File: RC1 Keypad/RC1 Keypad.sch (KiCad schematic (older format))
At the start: 24 parts

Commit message: Added RS/ST/SST to schematic
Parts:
- removed J?: KB, symbol Conn_02x05_Counter_Clockwise
- added D1: PWR, symbol LED_Small
- added J1: KB, symbol Conn_02x08_Counter_Clockwise
- added SW22: SST, symbol SW_SPST
- added SW23: RS, Button_Switch_Keyboard:SW_Cherry_MX_1.00u_PCB, symbol SW_Keyboard
- added SW24: ST, Button_Switch_Keyboard:SW_Cherry_MX_1.00u_PCB, symbol SW_Keyboard
- gave numbers to parts that had none: 23
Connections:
- net labels added: LED, RS, SST_IN, SST_OUT, ST, VCC
- wire segments 69 -> 85
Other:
- moved on the sheet: SW1, SW10, SW11, SW12, SW13, SW14, SW15, SW16, SW17, SW18, SW19, SW2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

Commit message: Keypad layout done
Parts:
- removed M1, M2: Mounting, Mounting:1pin, symbol Mounting
- D1: footprint (none) -> LEDs:LED_D5.0mm
- J1: footprint (none) -> Pin_Headers:Pin_Header_Straight_2x08_Pitch2.54mm
- SW22: footprint (none) -> Buttons_Switches_THT:SW_DIP_x1_W7.62mm_Slide
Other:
- note added: "RC-1 Hex keypad"
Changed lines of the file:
@@
 LIBS:valves
 LIBS:sw_keyboard
-LIBS:ZX Keyboard-cache
+LIBS:RC1 Keypad-cache
 EELAYER 25 0
 EELAYER END
@@
 Connection ~ 5225 4350
 $Comp
-L Mounting M2
-U 1 1 5D61DCEC
-P 11150 550
-F 0 "M2" H 11150 650 50  0001 C CNN
-F 1 "Mounting" H 11150 475 50  0001 C CNN
-F 2 "Mounting:1pin" H 11150 550 50  0001 C CNN
-F 3 "" H 11150 550 50  0001 C CNN
-	1    11150 550
-	1    0    0    -1
-$EndComp
-$Comp
-L Mounting M1
-U 1 1 5D61DCED
-P 11025 550
-F 0 "M1" H 11025 650 50  0001 C CNN
-F 1 "Mounting" H 11025 475 50  0001 C CNN
-F 2 "Mounting:1pin" H 11025 550 50  0001 C CNN
-F 3 "" H 11025 550 50  0001 C CNN
-	1    11025 550
-	1    0    0    -1
-$EndComp
-$Comp
 L SW_Keyboard SW13
 U 1 1 5D61DCC3
@@
 F 0 "SW22" H 6375 2350 50  0000 C CNN
 F 1 "SST" H 6375 2175 50  0000 C CNN
-F 2 "" H 6375 2225 50  0001 C CNN
+F 2 "Buttons_Switches_THT:SW_DIP_x1_W7.62mm_Slide" H 6375 2225 50  0001 C CNN
 F 3 "" H 6375 2225 50  0001 C CNN
 	1    6375 2225
@@
 F 0 "J1" H 5500 2775 50  0000 C CNN
 F 1 "KB" H 5500 2175 50  0000 C CNN
-F 2 "" H 5450 2525 50  0001 C CNN
+F 2 "Pin_Headers:Pin_Header_Straight_2x08_Pitch2.54mm" H 5450 2525 50  0001 C CNN
 F 3 "" H 5450 2525 50  0001 C CNN
 	1    5450 2525
@@
 F 0 "D1" H 6125 2475 50  0000 L CNN
 F 1 "PWR" H 6350 2475 50  0000 L CNN
-F 2 "" V 6275 2425 50  0001 C CNN
+F 2 "LEDs:LED_D5.0mm" V 6275 2425 50  0001 C CNN
 F 3 "" V 6275 2425 50  0001 C CNN
 	1    6275 2425
@@
 Wire Wire Line
 	6650 2225 6650 2325
+Text Notes 7350 7500 0    60   ~ 0
+RC-1 Hex keypad
 $EndSCHEMATC

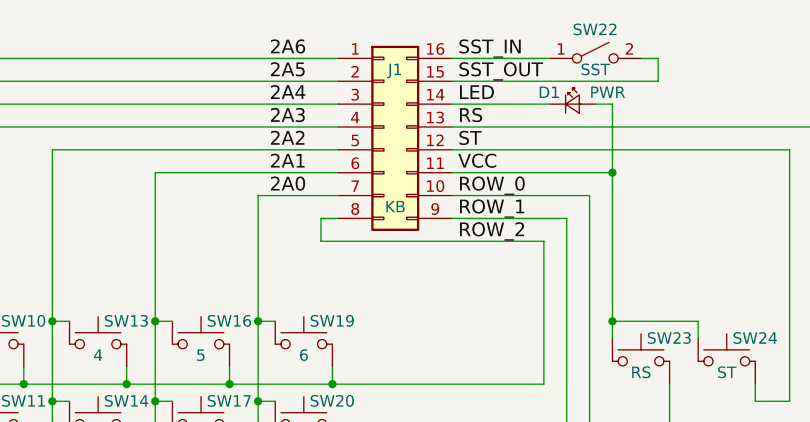
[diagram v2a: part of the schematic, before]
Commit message: Added UI signals to CPU board
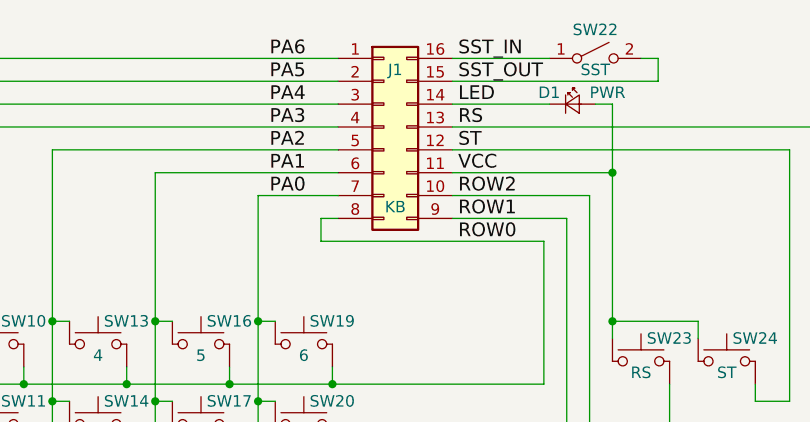
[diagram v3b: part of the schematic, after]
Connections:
- net 2A0 renamed PA0
- net 2A1 renamed PA1
- net 2A2 renamed PA2
- net 2A3 renamed PA3
- net 2A4 renamed PA4
- net 2A5 renamed PA5
- net 2A6 renamed PA6
- net ROW_0 renamed ROW2
- net ROW_1 renamed ROW1
- net ROW_2 renamed ROW0
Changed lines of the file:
@@
 	1    0    0    -1
 $EndComp
+Text Label 5775 3025 0    60   ~ 0
+ROW0
+Text Label 5775 2925 0    60   ~ 0
+ROW1
 Text Label 5775 2825 0    60   ~ 0
-ROW_0
-Text Label 5775 2925 0    60   ~ 0
-ROW_1
-Text Label 5775 3025 0    60   ~ 0
-ROW_2
+ROW2
 Wire Wire Line
 	2200 2225 5250 2225
@@
 	3550 2525 5250 2525
 Text Label 4950 2825 0    60   ~ 0
-2A0
+PA0
 Text Label 4950 2725 0    60   ~ 0
-2A1
+PA1
 Text Label 4950 2625 0    60   ~ 0
-2A2
+PA2
 Text Label 4950 2525 0    60   ~ 0
-2A3
+PA3
 Text Label 4950 2425 0    60   ~ 0
-2A4
+PA4
 Text Label 4950 2325 0    60   ~ 0
-2A5
+PA5
 Wire Wire Line
 	4000 2625 5250 2625
 Text Label 4950 2225 0    60   ~ 0
-2A6
+PA6
 $Comp
 L SW_Keyboard SW23

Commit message: Keypad SX layout done
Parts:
- removed SW22: SST, Buttons_Switches_THT:SW_DIP_x1_W7.62mm_Slide, symbol SW_SPST
- added M1, M2, M3, M4: Mounting, Mounting:1pin, symbol Mounting
- added SW22: SST, Pin_Headers:Pin_Header_Straight_1x03_Pitch2.54mm, symbol SW_SPDT
- SW1, SW10, SW11, SW12, SW13, SW14, SW15, SW16, SW17, SW18, SW19, SW2, SW20, SW21, SW23, SW24, SW3, SW4, SW5, SW6, SW7, SW8, SW9: footprint Button_Switch_Keyboard:SW_Cherry_MX_1.00u_PCB -> Buttons_Switches_THT:SW_PUSH_6mm
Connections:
- net SST_IN: now also SW22.2 (B)
- net SST_OUT: now also SW22.3 (C)
- no-connect marks 0 -> 1
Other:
- note added: "The keypad module for the RC One computer, has the classic KIM-1 layout with a\ncustom connector. This is the standard version using cheap tactile momentary buttons\nand is smaller [and cheaper to make] compared to the MX version."
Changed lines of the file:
@@
 LIBS:valves
 LIBS:sw_keyboard
+LIBS:mounting
 LIBS:RC1 Keypad-cache
 EELAYER 25 0
@@
 F 0 "SW16" H 4675 3575 50  0000 L CNN
 F 1 "5" H 4650 3425 50  0000 C CNN
-F 2 "Button_Switch_Keyboard:SW_Cherry_MX_1.00u_PCB" H 4650 3675 50  0001 C CNN
+F 2 "Buttons_Switches_THT:SW_PUSH_6mm" H 4650 3675 50  0001 C CNN
 F 3 "" H 4650 3675 50  0001 C CNN
 	1    4650 3475
@@
 F 0 "SW10" H 3775 3575 50  0000 L CNN
 F 1 "3" H 3750 3425 50  0000 C CNN
-F 2 "Button_Switch_Keyboard:SW_Cherry_MX_1.00u_PCB" H 3750 3675 50  0001 C CNN
+F 2 "Buttons_Switches_THT:SW_PUSH_6mm" H 3750 3675 50  0001 C CNN
 F 3 "" H 3750 3675 50  0001 C CNN
 	1    3750 3475
@@
 F 0 "SW7" H 3325 3575 50  0000 L CNN
 F 1 "2" H 3300 3425 50  0000 C CNN
-F 2 "Button_Switch_Keyboard:SW_Cherry_MX_1.00u_PCB" H 3300 3675 50  0001 C CNN
+F 2 "Buttons_Switches_THT:SW_PUSH_6mm" H 3300 3675 50  0001 C CNN
 F 3 "" H 3300 3675 50  0001 C CNN
 	1    3300 3475
@@
 F 0 "SW4" H 2875 3575 50  0000 L CNN
 F 1 "1" H 2850 3425 50  0000 C CNN
-F 2 "Button_Switch_Keyboard:SW_Cherry_MX_1.00u_PCB" H 2850 3675 50  0001 C CNN
+F 2 "Buttons_Switches_THT:SW_PUSH_6mm" H 2850 3675 50  0001 C CNN
 F 3 "" H 2850 3675 50  0001 C CNN
 	1    2850 3475
@@
 F 0 "SW12" H 3775 4275 50  0000 L CNN
 F 1 "DA" H 3750 4125 50  0000 C CNN
-F 2 "Button_Switch_Keyboard:SW_Cherry_MX_1.00u_PCB" H 3750 4375 50  0001 C CNN
+F 2 "Buttons_Switches_THT:SW_PUSH_6mm" H 3750 4375 50  0001 C CNN
 F 3 "" H 3750 4375 50  0001 C CNN
 	1    3750 4175
@@
 F 0 "SW3" H 2425 4275 50  0000 L CNN
 F 1 "E" H 2400 4125 50  0000 C CNN
-F 2 "Button_Switch_Keyboard:SW_Cherry_MX_1.00u_PCB" H 2400 4375 50  0001 C CNN
+F 2 "Buttons_Switches_THT:SW_PUSH_6mm" H 2400 4375 50  0001 C CNN
 F 3 "" H 2400 4375 50  0001 C CNN
 	1    2400 4175
@@
 F 0 "SW6" H 2875 4275 50  0000 L CNN
 F 1 "F" H 2850 4125 50  0000 C CNN
-F 2 "Button_Switch_Keyboard:SW_Cherry_MX_1.00u_PCB" H 2850 4375 50  0001 C CNN
+F 2 "Buttons_Switches_THT:SW_PUSH_6mm" H 2850 4375 50  0001 C CNN
 F 3 "" H 2850 4375 50  0001 C CNN
 	1    2850 4175
@@
 F 0 "SW20" H 5125 3925 50  0000 L CNN
 F 1 "D" H 5100 3775 50  0000 C CNN
-F 2 "Button_Switch_Keyboard:SW_Cherry_MX_1.00u_PCB" H 5100 4025 50  0001 C CNN
+F 2 "Buttons_Switches_THT:SW_PUSH_6mm" H 5100 4025 50  0001 C CNN
 F 3 "" H 5100 4025 50  0001 C CNN
 	1    5100 3825
@@
 F 0 "SW11" H 3775 3925 50  0000 L CNN
 F 1 "A" H 3750 3775 50  0000 C CNN
-F 2 "Button_Switch_Keyboard:SW_Cherry_MX_1.00u_PCB" H 3750 4025 50  0001 C CNN
+F 2 "Buttons_Switches_THT:SW_PUSH_6mm" H 3750 4025 50  0001 C CNN
 F 3 "" H 3750 4025 50  0001 C CNN
 	1    3750 3825
@@
 F 0 "SW19" H 5125 3575 50  0000 L CNN
 F 1 "6" H 5100 3425 50  0000 C CNN
-F 2 "Button_Switch_Keyboard:SW_Cherry_MX_1.00u_PCB" H 5100 3675 50  0001 C CNN
+F 2 "Buttons_Switches_THT:SW_PUSH_6mm" H 5100 3675 50  0001 C CNN
 F 3 "" H 5100 3675 50  0001 C CNN
 	1    5100 3475
@@
 F 0 "SW2" H 2425 3925 50  0000 L CNN
 F 1 "7" H 2400 3775 50  0000 C CNN
-F 2 "Button_Switch_Keyboard:SW_Cherry_MX_1.00u_PCB" H 2400 4025 50  0001 C CNN
+F 2 "Buttons_Switches_THT:SW_PUSH_6mm" H 2400 4025 50  0001 C CNN
 F 3 "" H 2400 4025 50  0001 C CNN
 	1    2400 3825
@@
 F 0 "SW5" H 2875 3925 50  0000 L CNN
 F 1 "8" H 2850 3775 50  0000 C CNN
-F 2 "Button_Switch_Keyboard:SW_Cherry_MX_1.00u_PCB" H 2850 4025 50  0001 C CNN
+F 2 "Buttons_Switches_THT:SW_PUSH_6mm" H 2850 4025 50  0001 C CNN
 F 3 "" H 2850 4025 50  0001 C CNN
 	1    2850 3825
@@
 F 0 "SW8" H 3325 3925 50  0000 L CNN
 F 1 "9" H 3300 3775 50  0000 C CNN
-F 2 "Button_Switch_Keyboard:SW_Cherry_MX_1.00u_PCB" H 3300 4025 50  0001 C CNN
+F 2 "Buttons_Switches_THT:SW_PUSH_6mm" H 3300 4025 50  0001 C CNN
 F 3 "" H 3300 4025 50  0001 C CNN
 	1    3300 3825
@@
 F 0 "SW1" H 2425 3575 50  0000 L CNN
 F 1 "Ø" H 2400 3425 50  0000 C CNN
-F 2 "Button_Switch_Keyboard:SW_Cherry_MX_1.00u_PCB" H 2400 3675 50  0001 C CNN
+F 2 "Buttons_Switches_THT:SW_PUSH_6mm" H 2400 3675 50  0001 C CNN
 F 3 "" H 2400 3675 50  0001 C CNN
 	1    2400 3475
@@
 F 0 "SW9" H 3325 4275 50  0000 L CNN
 F 1 "AD" H 3300 4125 50  0000 C CNN
-F 2 "Button_Switch_Keyboard:SW_Cherry_MX_1.00u_PCB" H 3300 4375 50  0001 C CNN
+F 2 "Buttons_Switches_THT:SW_PUSH_6mm" H 3300 4375 50  0001 C CNN
 F 3 "" H 3300 4375 50  0001 C CNN
 	1    3300 4175
@@
 F 0 "SW14" H 4225 3925 50  0000 L CNN
 F 1 "B" H 4200 3775 50  0000 C CNN
-F 2 "Button_Switch_Keyboard:SW_Cherry_MX_1.00u_PCB" H 4200 4025 50  0001 C CNN
+F 2 "Buttons_Switches_THT:SW_PUSH_6mm" H 4200 4025 50  0001 C CNN
 F 3 "" H 4200 4025 50  0001 C CNN
 	1    4200 3825
@@
 F 0 "SW17" H 4675 3925 50  0000 L CNN
 F 1 "C" H 4650 3775 50  0000 C CNN
-F 2 "Button_Switch_Keyboard:SW_Cherry_MX_1.00u_PCB" H 4650 4025 50  0001 C CNN
+F 2 "Buttons_Switches_THT:SW_PUSH_6mm" H 4650 4025 50  0001 C CNN
 F 3 "" H 4650 4025 50  0001 C CNN
 	1    4650 3825
@@
 F 0 "SW15" H 4225 4275 50  0000 L CNN
 F 1 "+" H 4200 4125 50  0000 C CNN
-F 2 "Button_Switch_Keyboard:SW_Cherry_MX_1.00u_PCB" H 4200 4375 50  0001 C CNN
+F 2 "Buttons_Switches_THT:SW_PUSH_6mm" H 4200 4375 50  0001 C CNN
 F 3 "" H 4200 4375 50  0001 C CNN
 	1    4200 4175
@@
 F 0 "SW18" H 4675 4275 50  0000 L CNN
 F 1 "GO" H 4650 4125 50  0000 C CNN
-F 2 "Button_Switch_Keyboard:SW_Cherry_MX_1.00u_PCB" H 4650 4375 50  0001 C CNN
+F 2 "Buttons_Switches_THT:SW_PUSH_6mm" H 4650 4375 50  0001 C CNN
 F 3 "" H 4650 4375 50  0001 C CNN
 	1    4650 4175
@@
 F 0 "SW21" H 5125 4275 50  0000 L CNN
 F 1 "PC" H 5100 4125 50  0000 C CNN
-F 2 "Button_Switch_Keyboard:SW_Cherry_MX_1.00u_PCB" H 5100 4375 50  0001 C CNN
+F 2 "Buttons_Switches_THT:SW_PUSH_6mm" H 5100 4375 50  0001 C CNN
 F 3 "" H 5100 4375 50  0001 C CNN
 	1    5100 4175
@@
 F 0 "SW13" H 4225 3575 50  0000 L CNN
 F 1 "4" H 4200 3425 50  0000 C CNN
-F 2 "Button_Switch_Keyboard:SW_Cherry_MX_1.00u_PCB" H 4200 3675 50  0001 C CNN
+F 2 "Buttons_Switches_THT:SW_PUSH_6mm" H 4200 3675 50  0001 C CNN
 F 3 "" H 4200 3675 50  0001 C CNN
 	1    4200 3475
@@
 F 0 "SW23" H 6600 3650 50  0000 L CNN
 F 1 "RS" H 6575 3500 50  0000 C CNN
-F 2 "Button_Switch_Keyboard:SW_Cherry_MX_1.00u_PCB" H 6575 3750 50  0001 C CNN
+F 2 "Buttons_Switches_THT:SW_PUSH_6mm" H 6575 3750 50  0001 C CNN
 F 3 "" H 6575 3750 50  0001 C CNN
 	1    6575 3550
@@
 F 0 "SW24" H 6975 3650 50  0000 L CNN
 F 1 "ST" H 6950 3500 50  0000 C CNN
-F 2 "Button_Switch_Keyboard:SW_Cherry_MX_1.00u_PCB" H 6950 3750 50  0001 C CNN
+F 2 "Buttons_Switches_THT:SW_PUSH_6mm" H 6950 3750 50  0001 C CNN
 F 3 "" H 6950 3750 50  0001 C CNN
 	1    6950 3550
@@
 	6825 3375 6450 3375
 Connection ~ 6450 3375
-$Comp
-L SW_SPST SW22
-U 1 1 5D62D132
-P 6375 2225
-F 0 "SW22" H 6375 2350 50  0000 C CNN
-F 1 "SST" H 6375 2175 50  0000 C CNN
-F 2 "Buttons_Switches_THT:SW_DIP_x1_W7.62mm_Slide" H 6375 2225 50  0001 C CNN
-F 3 "" H 6375 2225 50  0001 C CNN
-	1    6375 2225
-	1    0    0    -1
-$EndComp
 $Comp
 L Conn_02x08_Counter_Clockwise J1
@@
 	5750 2225 6175 2225
 Wire Wire Line
-	5750 2325 6650 2325
+	5750 2325 6725 2325
 Text Label 5775 2725 0    60   ~ 0
 VCC
@@
 Text Label 5775 2325 0    60   ~ 0
 SST_OUT
-Wire Wire Line
-	6575 2225 6650 2225
-Wire Wire Line
-	6650 2225 6650 2325
 Text Notes 7350 7500 0    60   ~ 0
 RC-1 Hex keypad
+Text Notes 7000 6825 0    60   ~ 0
+The keypad module for the RC One computer, has the classic KIM-1 layout with a\ncustom connector. This is the standard version using cheap tactile momentary buttons\nand is smaller [and cheaper to make] compared to the MX version.
+$Comp
+L Mounting M4
+U 1 1 5D726697
+P 11150 550
+F 0 "M4" H 11150 650 50  0001 C CNN
+F 1 "Mounting" H 11150 475 50  0001 C CNN
+F 2 "Mounting:1pin" H 11150 550 50  0001 C CNN
+F 3 "" H 11150 550 50  0001 C CNN
+	1    11150 550
+	1    0    0    -1
+$EndComp
+$Comp
+L Mounting M3
+U 1 1 5D72672B
+P 11025 550
+F 0 "M3" H 11025 650 50  0001 C CNN
+F 1 "Mounting" H 11025 475 50  0001 C CNN
+F 2 "Mounting:1pin" H 11025 550 50  0001 C CNN
+F 3 "" H 11025 550 50  0001 C CNN
+	1    11025 550
+	1    0    0    -1
+$EndComp
+$Comp
+L Mounting M2
+U 1 1 5D726784
+P 10900 550
+F 0 "M2" H 10900 650 50  0001 C CNN
+F 1 "Mounting" H 10900 475 50  0001 C CNN
+F 2 "Mounting:1pin" H 10900 550 50  0001 C CNN
+F 3 "" H 10900 550 50  0001 C CNN
+	1    10900 550
+	1    0    0    -1
+$EndComp
+$Comp
+L Mounting M1
+U 1 1 5D7267DD
+P 10775 550
+F 0 "M1" H 10775 650 50  0001 C CNN
+F 1 "Mounting" H 10775 475 50  0001 C CNN
+F 2 "Mounting:1pin" H 10775 550 50  0001 C CNN
+F 3 "" H 10775 550 50  0001 C CNN
+	1    10775 550
+	1    0    0    -1
+$EndComp
+$Comp
+L SW_SPDT SW22
+U 1 1 5D726F83
+P 6450 2075
+F 0 "SW22" H 6450 2245 50  0000 C CNN
+F 1 "SST" H 6450 1875 50  0000 C CNN
+F 2 "Pin_Headers:Pin_Header_Straight_1x03_Pitch2.54mm" H 6450 2075 50  0001 C CNN
+F 3 "" H 6450 2075 50  0001 C CNN
+	1    6450 2075
+	1    0    0    -1
+$EndComp
+Wire Wire Line
+	6175 2225 6175 2075
+Wire Wire Line
+	6175 2075 6250 2075
+Wire Wire Line
+	6650 2175 6725 2175
+Wire Wire Line
+	6725 2175 6725 2325
+NoConn ~ 6650 1975
 $EndSCHEMATC

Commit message: Updated keypad schematic for clarity
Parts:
- J1: value KB -> KEYPAD; symbol Conn_02x08_Counter_Clockwise -> RC1_Keypad_Port
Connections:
- net LED: no longer names the net of D1.1 (K), J1.14 (Pin_14)
- net RS: no longer names the net of J1.13 (Pin_13), SW23.2
- net SST_IN: no longer names the net of J1.16 (Pin_16), SW22.2 (B)
- net SST_OUT: no longer names the net of J1.15 (Pin_15), SW22.3 (C)
- net ST: no longer names the net of J1.12 (Pin_12), SW24.2
- net VCC: no longer names the net of D1.2 (A), J1.11 (Pin_11), SW23.1, SW24.1
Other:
- note added: "B"
- moved on the sheet: D1, SW1, SW10, SW11, SW12, SW13, SW14, SW15, SW16, SW17, SW18, SW19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
